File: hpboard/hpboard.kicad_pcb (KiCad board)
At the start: 2 copper layers, 60 x 100 mm, 32 parts, among them Q1 T2N7002AK, Q2 T2N7002AK, Q3 Si4435FDY, Q4 Si4435FDY, SW1 FSM2JAH, U1 TMCS1108A4B, U2 ATtiny1604-SS, U3 TLV1117-50

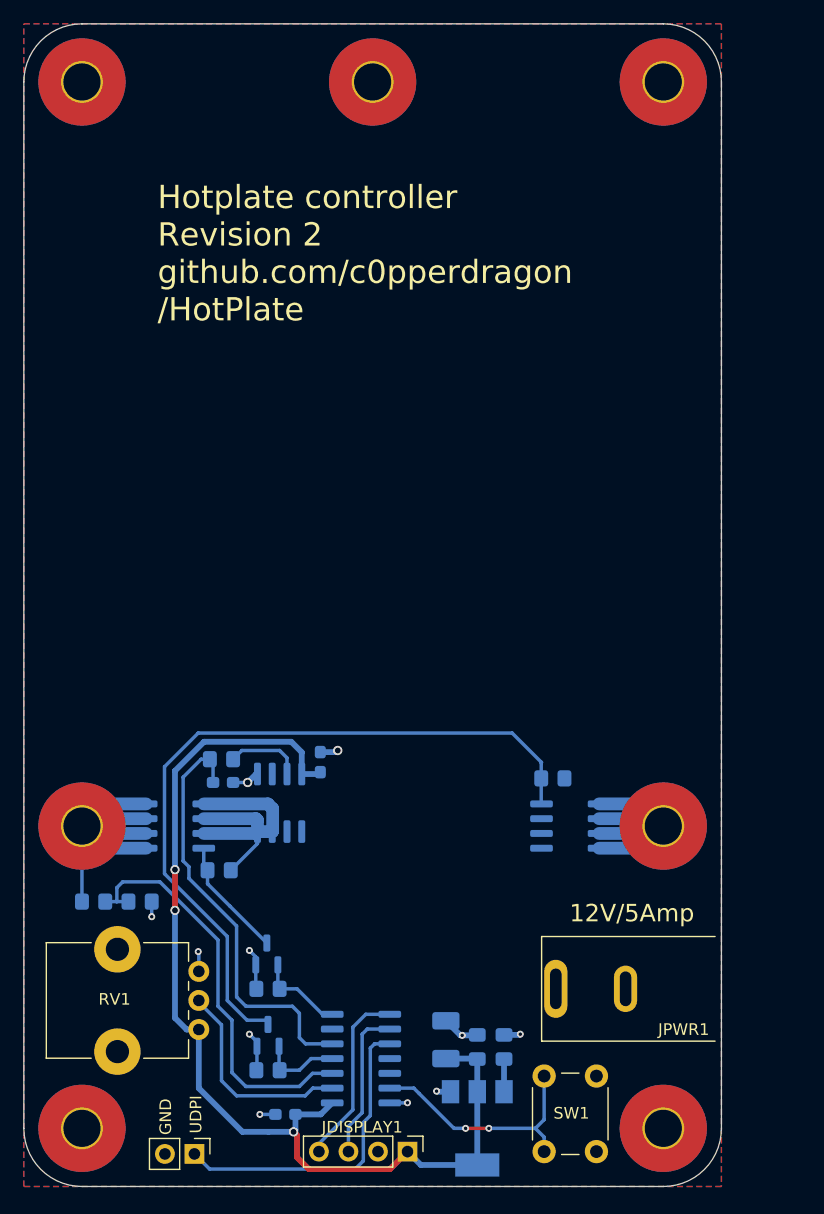
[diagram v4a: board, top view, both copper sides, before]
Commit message: Rework PCB for better soldering
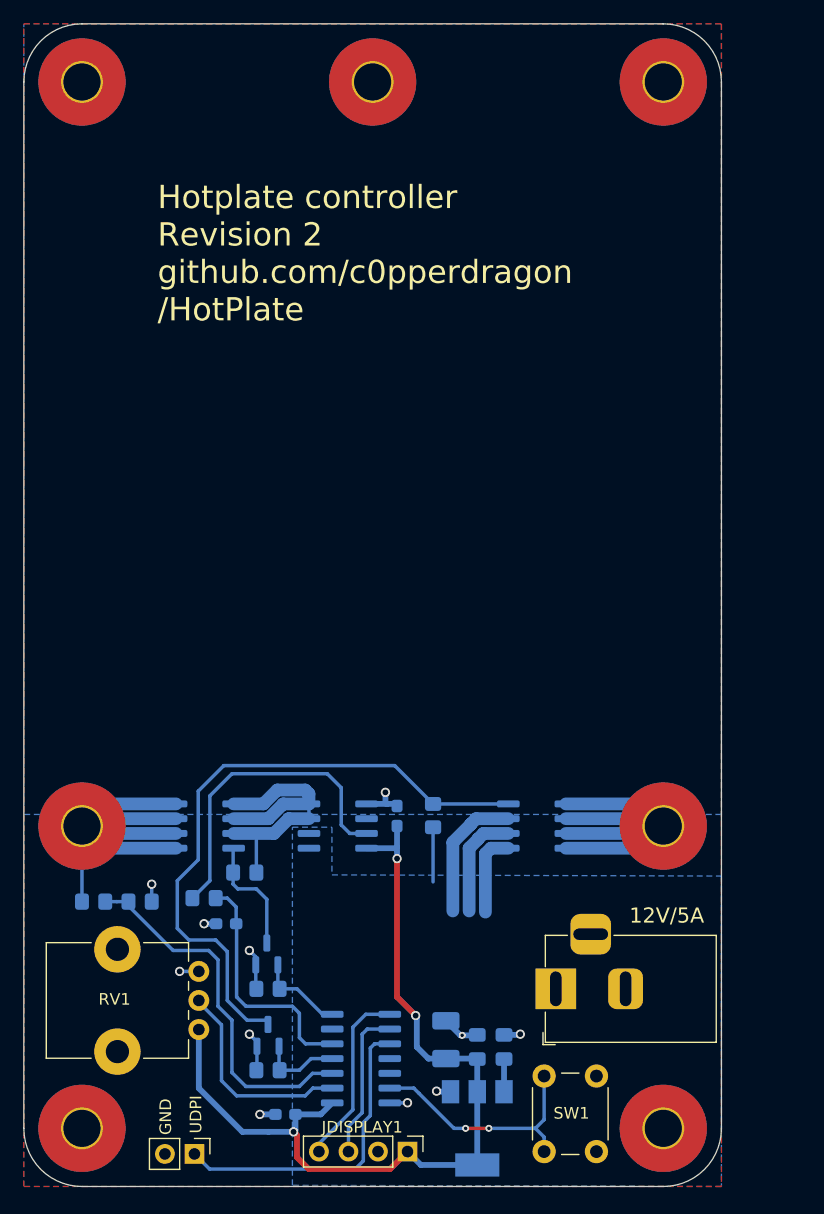
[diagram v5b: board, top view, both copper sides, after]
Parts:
- JPWR1: value PJ-037BH -> Barrel_Jack_Switch; footprint Library:PJ_037BH -> Connector_BarrelJack:BarrelJack_Horizontal
- moved C6 12.2 mm to (117.4, 125.4), turned to 180 degrees
- moved R9 12.0 mm to (115.5, 123.2), turned to 0 degrees
- moved R4 10.8 mm to (135.2, 116.1), turned to 90 degrees
- moved C5 8.07 mm to (132.1, 116.1)
- moved U1 5.39 mm to (127.0, 117.0), turned to 0 degrees
- moved Q4 2.85 mm to (144.1, 117.0)
- moved Q3 2.57 mm to (115.6, 117.0)
- moved R3 2.21 mm to (119.0, 121.0)
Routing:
- net /12V: track 2.81 -> 35.5 mm
- net Net-(R9-Pad1): track 6.60 -> 27.7 mm
- net /SENSE_CURRENT: track 37.0 -> 21.0 mm
- net +5V: track 90.4 -> 76.2 mm
- net /BOTTOM: track 24.2 -> 35.6 mm
- net /TOP: track 30.7 -> 41.0 mm
- net Net-(Q2-Pad3): track 65.0 -> 55.3 mm
- net /SENSE_VOLTAGE: track 35.7 -> 31.8 mm
- net Net-(Q3-Pad1): track 24.0 -> 26.6 mm
- net GND: track 22.5 -> 23.4 mm
- added copper zone on B.Cu, net (none)
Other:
- board text added: "12V/5A"
- board text removed: "12V/5Amp"

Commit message: Add hole to PCB to allow the hotplate to SMD-solder its own clone. Switch GND and VCC on display module to support slimmer and more common variant
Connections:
- JDISPLAY1 pad 1: +5V -> GND
- JDISPLAY1 pad 2: GND -> +5V
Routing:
- net +5V: track 76.2 -> 76.8 mm
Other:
- outline, holes or cut-outs redrawn
- board text added: "Hotplate controller Revision 3 github.com/c0pperdragon /HotPlate"
- board text removed: "Hotplate controller Revision 2 github.com/c0pperdragon /HotPlate"
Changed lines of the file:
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@@
   )
   (paper "A4")
+  (title_block
+    (title "Hot Plate controller")
+    (rev "3")
+  )
   (layers
     (0 "F.Cu" signal)
@@
     (pad_to_mask_clearance 0)
     (pcbplotparams
-      (layerselection 0x00010f0_ffffffff)
+      (layerselection 0x00010f4_ffffffff)
       (disableapertmacros false)
       (usegerberextensions false)
@@
     (fp_line (start 1.27 8.89) (end -1.27 8.89) (layer "F.Fab") (width 0.1))
     (pad "1" thru_hole rect (at 0 0 270) (size 1.7 1.7) (drill 1) (layers *.Cu *.Mask)
-      (net 1 "+5V") (pinfunction "Pin_1") (pintype "passive"))
+      (net 2 "GND") (pinfunction "Pin_1") (pintype "passive"))
     (pad "2" thru_hole oval (at 0 2.54 270) (size 1.7 1.7) (drill 1) (layers *.Cu *.Mask)
-      (net 2 "GND") (pinfunction "Pin_2") (pintype "passive"))
+      (net 1 "+5V") (pinfunction "Pin_2") (pintype "passive"))
     (pad "3" thru_hole oval (at 0 5.08 270) (size 1.7 1.7) (drill 1) (layers *.Cu *.Mask)
       (net 5 "/SCL") (pinfunction "Pin_3") (pintype "passive"))
@@
     (fp_line (start -1 0.625) (end 1 0.625) (layer "B.Fab") (width 0.1))
     (fp_line (start 1 0.625) (end 1 -0.625) (layer "B.Fab") (width 0.1))
-    (pad "1" smd roundrect (at -1 0) (size 1.2 1.4) (layers "B.Cu" "B.Paste" "B.Mask") (roundrect_rratio 0.208333)
+    (pad "1" smd roundrect (at -1 0) (size 1.2 1.4) (layers "B.Cu" "B.Paste" "B.Mask") (roundrect_rratio 0.2083333333)
       (net 26 "Net-(R9-Pad1)") (pintype "passive"))
-    (pad "2" smd roundrect (at 1 0) (size 1.2 1.4) (layers "B.Cu" "B.Paste" "B.Mask") (roundrect_rratio 0.208333)
+    (pad "2" smd roundrect (at 1 0) (size 1.2 1.4) (layers "B.Cu" "B.Paste" "B.Mask") (roundrect_rratio 0.2083333333)
       (net 14 "/SENSE_CURRENT") (pintype "passive"))
     (model "${KICAD6_3DMODEL_DIR}/Resistor_SMD.3dshapes/R_0805_2012Metric.wrl"
@@
     (fp_line (start -1.75 -1.4) (end 1.75 -1.4) (layer "B.Fab") (width 0.1))
     (fp_line (start -1.05 1.4) (end -1.75 0.7) (layer "B.Fab") (width 0.1))
-    (pad "1" smd roundrect (at -1.625 0 90) (size 1.5 2.35) (layers "B.Cu" "B.Paste" "B.Mask") (roundrect_rratio 0.166667)
+    (pad "1" smd roundrect (at -1.625 0 90) (size 1.5 2.35) (layers "B.Cu" "B.Paste" "B.Mask") (roundrect_rratio 0.1666673333)
       (net 1 "+5V") (pintype "passive"))
-    (pad "2" smd roundrect (at 1.625 0 90) (size 1.5 2.35) (layers "B.Cu" "B.Paste" "B.Mask") (roundrect_rratio 0.166667)
+    (pad "2" smd roundrect (at 1.625 0 90) (size 1.5 2.35) (layers "B.Cu" "B.Paste" "B.Mask") (roundrect_rratio 0.1666673333)
       (net 2 "GND") (pintype "passive"))
     (model "${KICAD6_3DMODEL_DIR}/Capacitor_Tantalum_SMD.3dshapes/CP_EIA-3528-21_Kemet-B.wrl"
@@
   (gr_arc (start 160 143) (mid 158.535534 146.535534) (end 155 148) (layer "Edge.Cuts") (width 0.1))
   (gr_arc (start 100 53) (mid 101.464466 49.464466) (end 105 48) (layer "Edge.Cuts") (width 0.1))
+  (gr_circle (center 130 93) (end 130 88) (layer "Edge.Cuts") (width 0.1) (fill none))
   (gr_line (start 160 53) (end 160 143) (layer "Edge.Cuts") (width 0.1))
   (gr_line (start 100 143) (end 100 53) (layer "Edge.Cuts") (width 0.1))
-  (gr_text "Hotplate controller \nRevision 2\ngithub.com/c0pperdragon\n/HotPlate\n" (at 111.5 67.75) (layer "F.SilkS")
+  (gr_text "Hotplate controller \nRevision 3\ngithub.com/c0pperdragon\n/HotPlate\n" (at 111.5 67.75) (layer "F.SilkS")
     (effects (font (size 2 2) (thickness 0.15)) (justify left))
   )
@@
   )
   (segment (start 123.5 145.5) (end 123.5 143.6) (width 0.5) (layer "F.Cu") (net 1))
-  (segment (start 131.5 146.5) (end 133 145) (width 0.5) (layer "F.Cu") (net 1))
   (segment (start 132.1 131.7) (end 132.1 119.8) (width 0.5) (layer "F.Cu") (net 1))
+  (segment (start 130.46 145) (end 128.96 146.5) (width 0.5) (layer "F.Cu") (net 1))
   (segment (start 133.7 133.3) (end 132.1 131.7) (width 0.5) (layer "F.Cu") (net 1))
+  (segment (start 124.5 146.5) (end 128.9 146.5) (width 0.5) (layer "F.Cu") (net 1))
   (segment (start 123.5 145.5) (end 124.5 146.5) (width 0.5) (layer "F.Cu") (net 1))
-  (segment (start 124.5 146.5) (end 131.5 146.5) (width 0.5) (layer "F.Cu") (net 1))
   (segment (start 123.5 143.6) (end 123.2 143.3) (width 0.5) (layer "F.Cu") (net 1))
+  (segment (start 128.96 146.5) (end 128.9 146.5) (width 0.5) (layer "F.Cu") (net 1))
   (via (at 133.7 133.3) (size 0.8) (drill 0.5) (layers "F.Cu" "B.Cu") (net 1))
   (via (at 123.2 143.3) (size 0.8) (drill 0.5) (layers "F.Cu" "B.Cu") (net 1))
   (via (at 132.1 119.8) (size 0.8) (drill 0.5) (layers "F.Cu" "B.Cu") (net 1))
-  (segment (start 134.15 146.15) (end 133 145) (width 0.5) (layer "B.Cu") (net 1))
   (segment (start 133.8 136) (end 134.8 137) (width 0.5) (layer "B.Cu") (net 1))
   (segment (start 132.1 119.8) (end 132.1 118.8) (width 0.5) (layer "B.Cu") (net 1))
   (segment (start 115.05 134.5) (end 115.05 139.55) (width 0.5) (layer "B.Cu") (net 1))
   (segment (start 136.3 137) (end 138.9625 137) (width 0.5) (layer "B.Cu") (net 1))
+  (segment (start 131.6 146.6) (end 138.55 146.6) (width 0.5) (layer "B.Cu") (net 1))
   (segment (start 115.05 139.55) (end 118.8 143.3) (width 0.5) (layer "B.Cu") (net 1))
   (segment (start 121.05 143.3) (end 123.2 143.3) (width 0.5) (layer "B.Cu") (net 1))
+  (segment (start 130.46 145) (end 130.46 145.46) (width 0.5) (layer "B.Cu") (net 1))
   (segment (start 139 139.85) (end 139 137.0375) (width 0.5) (layer "B.Cu") (net 1))
   (segment (start 123.3625 143.1375) (end 123.3625 141.8) (width 0.5) (layer "B.Cu") (net 1))
+  (segment (start 138.55 146.6) (end 139 146.15) (width 0.5) (layer "B.Cu") (net 1))
   (segment (start 132.1 118.8) (end 132.1 117) (width 0.5) (layer "B.Cu") (net 1))
   (segment (start 123.5375 141.8) (end 125.535 141.8) (width 0.5) (layer "B.Cu") (net 1))
-  (segment (start 139 146.15) (end 134.15 146.15) (width 0.5) (layer "B.Cu") (net 1))
+  (segment (start 130.46 145.46) (end 131.6 146.6) (width 0.5) (layer "B.Cu") (net 1))
   (segment (start 129.475 118.905) (end 131.995 118.905) (width 0.5) (layer "B.Cu") (net 1))
   (segment (start 134.8 137) (end 136.3 137) (width 0.5) (layer "B.Cu") (net 1))
@@
   (segment (start 129.475 117.635) (end 128.035 117.635) (width 0.3) (layer "B.Cu") (net 26))
   (segment (start 116 121.7) (end 114.5 123.2) (width 0.3) (layer "B.Cu") (net 26))
+  (zone (net 0) (net_name "") (layers "F.Cu" "Edge.Cuts") (hatch edge 0.508)
+    (connect_pads (clearance 0))
+    (min_thickness 0.254)
+    (keepout (tracks not_allowed) (vias not_allowed) (pads not_allowed) (copperpour not_allowed) (footprints allowed))
+    (fill (thermal_gap 0.508) (thermal_bridge_width 0.508))
+    (polygon
+      (pts
+        (xy 157 101)
+        (xy 103 101)
+        (xy 103 100)
+        (xy 157 100)
+      )
+    )
+  )
   (zone (net 2) (net_name "GND") (layer "F.Cu") (hatch edge 0.508)
     (connect_pads yes (clearance 0.508))
@@
         (xy 160 116)
         (xy 100 116)
-        (xy 100 48)
-        (xy 160 48)
+        (xy 100 101)
+        (xy 160 101)
       )
     )
